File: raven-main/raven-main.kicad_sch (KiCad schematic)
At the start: 2 parts, among them U1 TLV3201AIDCKT

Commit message: Created detector circuit
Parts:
- removed D1: BPW34, OptoDevice:Osram_DIL2_4.3x4.65mm_P5.08mm, symbol Sensor_Optical:BPW34
- removed U1: TLV3201AIDCKT, TLV3201AIDCKT:SOT65P210X110-5N, symbol TLV3201AIDCKT:TLV3201AIDCKT
- added U3: ESP32-S3, Package_DFN_QFN:QFN-56-1EP_7x7mm_P0.4mm_EP4x4mm, symbol MCU_Espressif:ESP32-S3
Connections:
- new net: U3.2 (VDD3P3), U3.3 (VDD3P3)
- new net 5V: U3.55 (VDDA), U3.56 (VDDA)
- new net GND: U3.57 (GND)
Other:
- added sheet Detector (raven-detector.kicad_sch)
- added sheet Power (raven-power.kicad_sch)

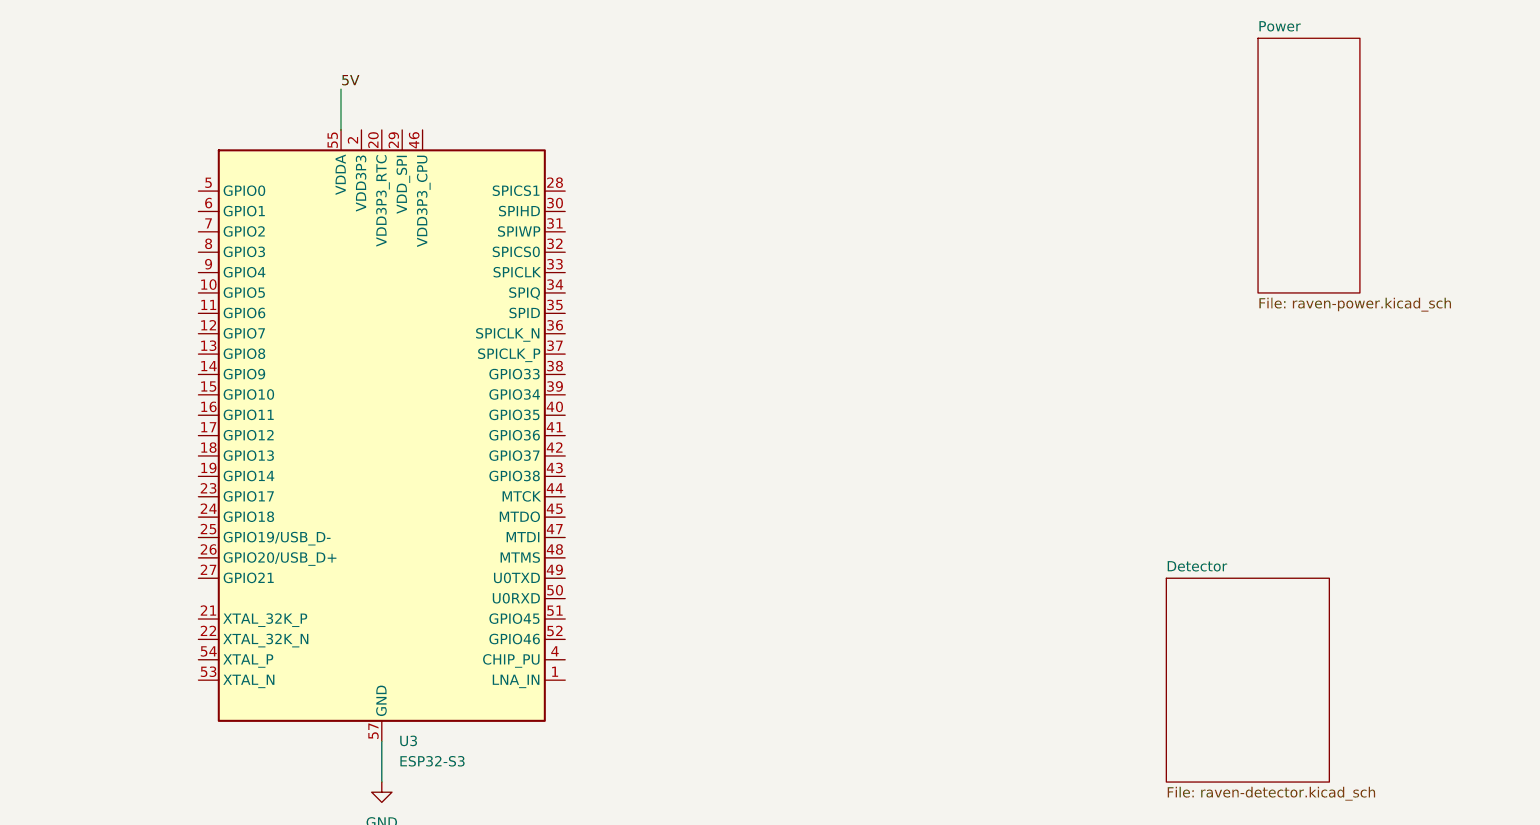
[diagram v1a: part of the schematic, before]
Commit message: Added LDO Regulator
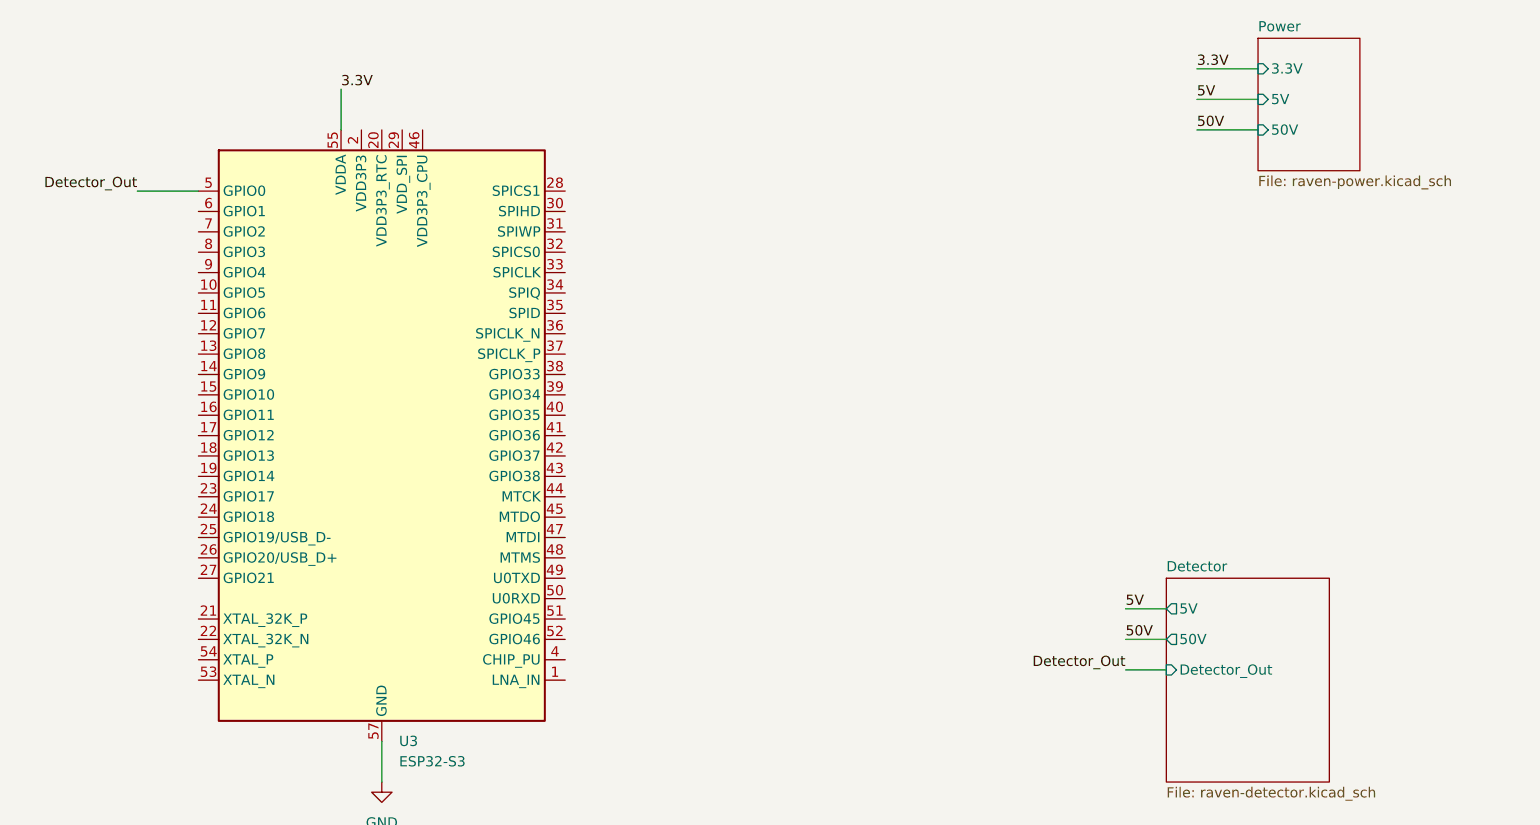
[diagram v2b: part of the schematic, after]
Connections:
- net 5V: no longer U3.55 (VDDA), U3.56 (VDDA)
- net Detector_Out: now reaches U3.5 (GPIO0)
- new net 3.3V: U3.55 (VDDA), U3.56 (VDDA)
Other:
- sheet Detector ports: added 50V, 5V, Detector_Out; removed none
- sheet Power ports: added 3.3V, 50V, 5V; removed none
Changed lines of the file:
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@@
+	(wire
+		(pts
+			(xy 232.41 43.18) (xy 240.03 43.18)
+		)
+		(stroke
+			(width 0)
+			(type default)
+		)
+	)
+	(wire
+		(pts
+			(xy 232.41 46.99) (xy 240.03 46.99)
+		)
+		(stroke
+			(width 0)
+			(type default)
+		)
+	)
 	(wire
 		(pts
@@
 	(wire
 		(pts
+			(xy 223.52 110.49) (xy 228.6 110.49)
+		)
+		(stroke
+			(width 0)
+			(type default)
+		)
+	)
+	(wire
+		(pts
+			(xy 223.52 106.68) (xy 228.6 106.68)
+		)
+		(stroke
+			(width 0)
+			(type default)
+		)
+	)
+	(wire
+		(pts
+			(xy 223.52 114.3) (xy 228.6 114.3)
+		)
+		(stroke
+			(width 0)
+			(type default)
+		)
+	)
+	(wire
+		(pts
 			(xy 125.73 41.91) (xy 125.73 46.99)
 		)
@@
 		)
 	)
+	(wire
+		(pts
+			(xy 100.33 54.61) (xy 107.95 54.61)
+		)
+		(stroke
+			(width 0)
+			(type default)
+		)
+	)
+	(wire
+		(pts
+			(xy 232.41 39.37) (xy 240.03 39.37)
+		)
+		(stroke
+			(width 0)
+			(type default)
+		)
+	)
+	(label "3.3V"
+		(at 232.41 39.37 0)
+		(effects
+			(font
+				(size 1.27 1.27)
+			)
+			(justify left bottom)
+		)
+	)
 	(label "5V"
+		(at 223.52 106.68 0)
+		(effects
+			(font
+				(size 1.27 1.27)
+			)
+			(justify left bottom)
+		)
+	)
+	(label "5V"
+		(at 232.41 43.18 0)
+		(effects
+			(font
+				(size 1.27 1.27)
+			)
+			(justify left bottom)
+		)
+	)
+	(label "50V"
+		(at 232.41 46.99 0)
+		(effects
+			(font
+				(size 1.27 1.27)
+			)
+			(justify left bottom)
+		)
+	)
+	(label "Detector_Out"
+		(at 223.52 114.3 180)
+		(effects
+			(font
+				(size 1.27 1.27)
+			)
+			(justify right bottom)
+		)
+	)
+	(label "3.3V"
 		(at 125.73 41.91 0)
+		(effects
+			(font
+				(size 1.27 1.27)
+			)
+			(justify left bottom)
+		)
+	)
+	(label "Detector_Out"
+		(at 100.33 54.61 180)
+		(effects
+			(font
+				(size 1.27 1.27)
+			)
+			(justify right bottom)
+		)
+	)
+	(label "50V"
+		(at 223.52 110.49 0)
 		(effects
 			(font
@@
 			)
 		)
+		(pin "5V" output
+			(at 228.6 106.68 180)
+			(effects
+				(font
+					(size 1.27 1.27)
+				)
+				(justify left)
+			)
+		)
+		(pin "50V" output
+			(at 228.6 110.49 180)
+			(effects
+				(font
+					(size 1.27 1.27)
+				)
+				(justify left)
+			)
+		)
+		(pin "Detector_Out" input
+			(at 228.6 114.3 180)
+			(effects
+				(font
+					(size 1.27 1.27)
+				)
+				(justify left)
+			)
+		)
 		(instances
 			(project "raven-main"
@@
 	(sheet
 		(at 240.03 35.56)
-		(size 12.7 31.75)
+		(size 12.7 16.51)
 		(exclude_from_sim no)
 		(in_bom yes)
@@
 		)
 		(property "Sheetfile" "raven-power.kicad_sch"
-			(at 240.03 67.8946 0)
+			(at 240.03 52.6546 0)
 			(show_name no)
 			(do_not_autoplace no)
@@
 			)
 		)
+		(pin "3.3V" input
+			(at 240.03 39.37 180)
+			(effects
+				(font
+					(size 1.27 1.27)
+				)
+				(justify left)
+			)
+		)
+		(pin "5V" input
+			(at 240.03 43.18 180)
+			(effects
+				(font
+					(size 1.27 1.27)
+				)
+				(justify left)
+			)
+		)
+		(pin "50V" input
+			(at 240.03 46.99 180)
+			(effects
+				(font
+					(size 1.27 1.27)
+				)
+				(justify left)
+			)
+		)

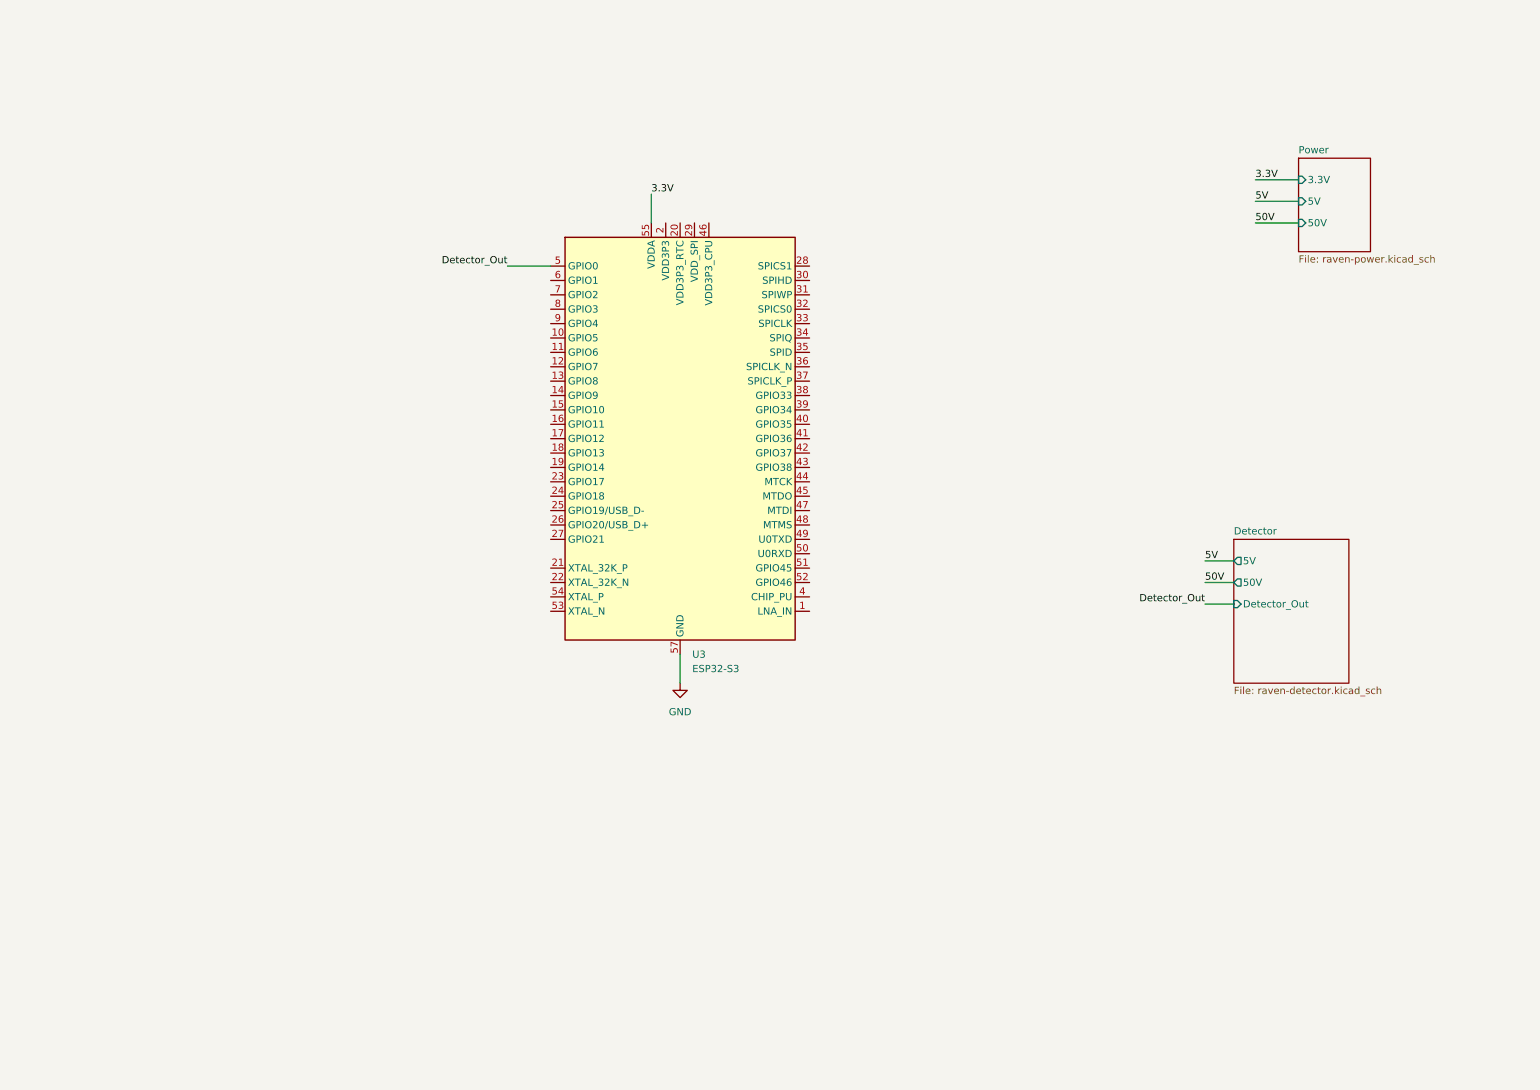
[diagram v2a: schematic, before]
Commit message: Used the ESP-32 board template to create full board
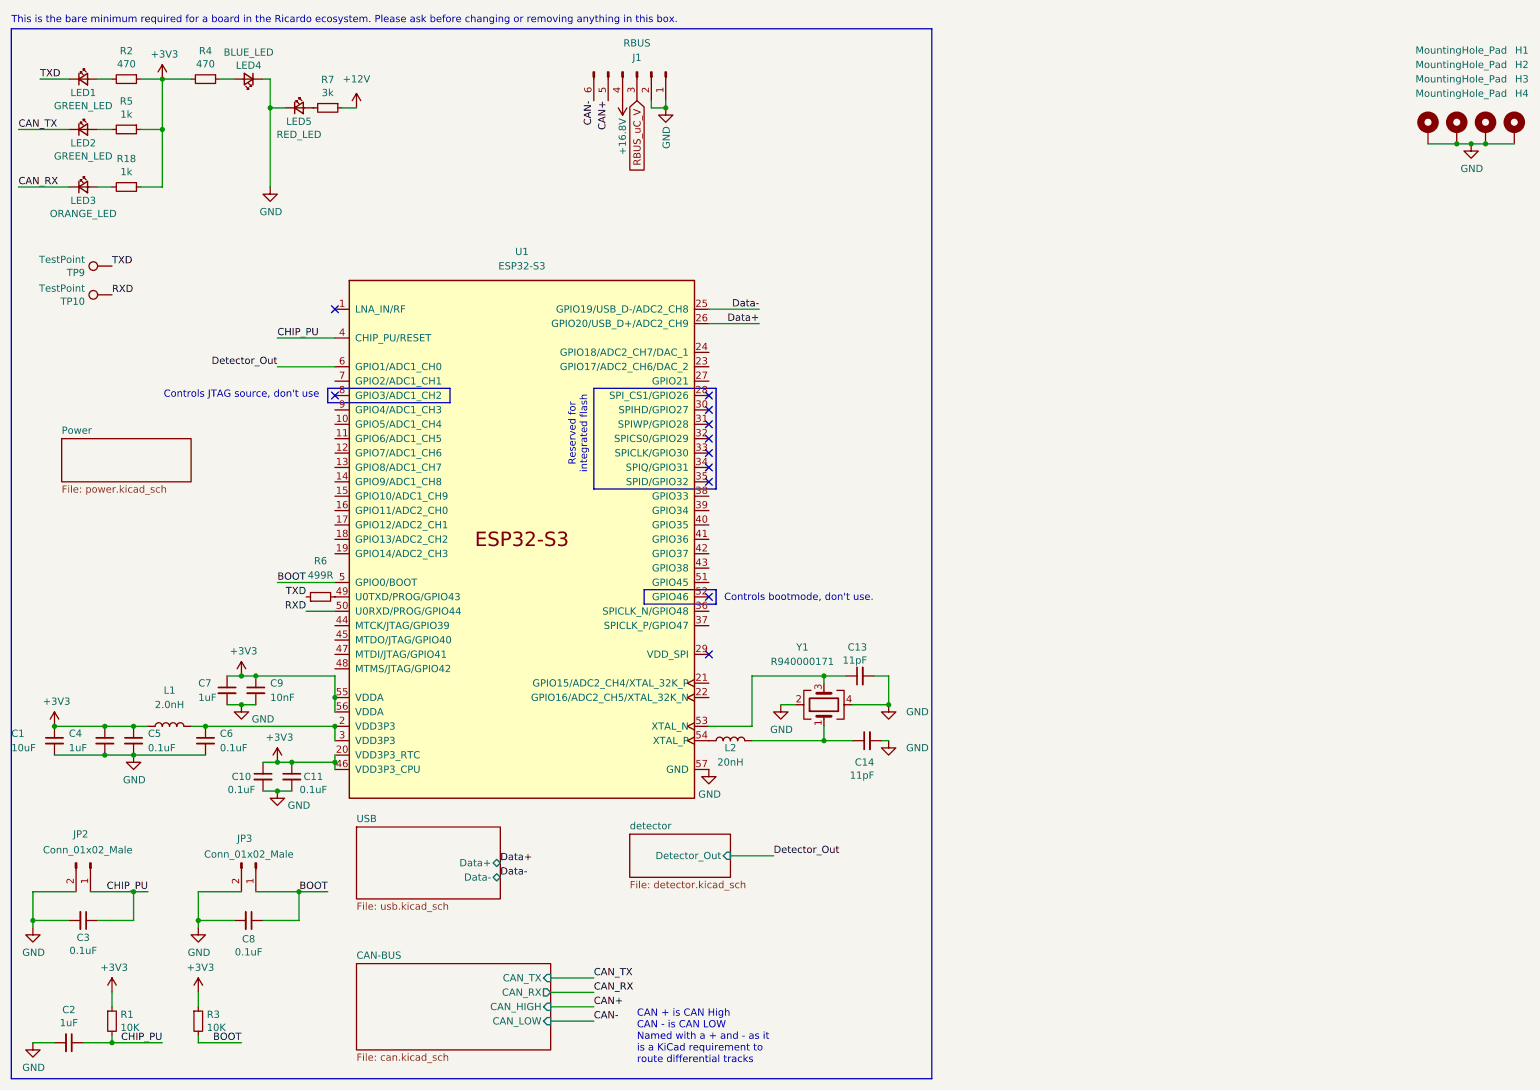
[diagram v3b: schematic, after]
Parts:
- removed U3: ESP32-S3, Package_DFN_QFN:QFN-56-1EP_7x7mm_P0.4mm_EP4x4mm, symbol MCU_Espressif:ESP32-S3
- added C1: 10uF, Capacitor_SMD:C_0402_1005Metric, symbol Device:C_Small
- added C10, C11, C3, C5, C6, C8: 0.1uF, Capacitor_SMD:C_0402_1005Metric, symbol Device:C_Small
- added C13, C14: 11pF, Capacitor_SMD:C_0402_1005Metric, symbol Device:C_Small
- added C2, C4, C7: 1uF, Capacitor_SMD:C_0402_1005Metric, symbol Device:C_Small
- added C9: 10nF, Capacitor_SMD:C_0402_1005Metric, symbol Device:C_Small
- added H1, H2, H3, H4: MountingHole_Pad, MountingHole:MountingHole_3.2mm_M3_DIN965_Pad, symbol Mechanical:MountingHole_Pad
- added J1: RBUS, iclr:Molex_Mini-Fit_Jr_5569-06A2_2x03_P4.20mm_Horizontal, symbol Connector:Conn_01x06_Male
- added JP2, JP3: Conn_01x02_Male, Connector_PinHeader_2.54mm:PinHeader_1x02_P2.54mm_Vertical, symbol Connector:Conn_01x02_Male
- added L1: 2.0nH, Inductor_SMD:L_0402_1005Metric, symbol Device:L
- added L2: 20nH, Inductor_SMD:L_0402_1005Metric, symbol Device:L
- added LED1, LED2: GREEN_LED, LED_SMD:LED_0402_1005Metric, symbol Device:LED_Small
- added LED3: ORANGE_LED, LED_SMD:LED_0402_1005Metric, symbol Device:LED_Small
- added LED4: BLUE_LED, LED_SMD:LED_0402_1005Metric, symbol Device:LED_Small
- added LED5: RED_LED, LED_SMD:LED_0402_1005Metric, symbol Device:LED_Small
- added R1, R3: 10K, Resistor_SMD:R_0402_1005Metric, symbol Device:R_Small
- added R18, R5: 1k, Resistor_SMD:R_0402_1005Metric, symbol Device:R_Small
- added R2, R4: 470, Resistor_SMD:R_0402_1005Metric, symbol Device:R_Small
- added R6: 499R, Resistor_SMD:R_0402_1005Metric, symbol Device:R_Small
- added R7: 3k, Resistor_SMD:R_0402_1005Metric, symbol Device:R_Small
- added TP10, TP9: TestPoint, TestPoint:TestPoint_Pad_D1.0mm, symbol Connector:TestPoint
- added U1: ESP32-S3, iclr:QFN40P700X700X90-57N, symbol Espressif:ESP32-S3
- added Y1: R940000171, iclr:Crystal_SMD_2016-4Pin_2.0x1.6mm, symbol Device:Crystal_GND24
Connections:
- net Detector_Out: now also U1.6 (GPIO1/ADC1_CH0)
- net GND: now also C1.2, C10.2, C11.2, C13.2, C14.2, C2.2, C3.2, C4.2, C5.2, C6.2, C7.2, C8.2, C9.2, H1.1, H2.1, H3.1, H4.1, J1.1 (Pin_1), J1.2 (Pin_2), JP2.2 (Pin_2), JP3.2 (Pin_2), LED4.1 (K), LED5.1 (K), U1.57 (GND), Y1.2, Y1.4
- new net: LED1.2 (A), R2.2
- new net: LED4.2 (A), R4.1
- new net: LED5.2 (A), R7.2
- new net: LED2.2 (A), R5.2
- new net: LED3.2 (A), R18.2
- new net: C14.1, L2.2, Y1.1
- new net: C13.1, U1.53 (XTAL_N), Y1.3
- new net: L2.1, U1.54 (XTAL_P)
- new net: C6.1, L1.2, U1.2 (VDD3P3), U1.3 (VDD3P3)
- new net: R6.2, U1.49 (U0TXD/PROG/GPIO43)
- new net +12V: R7.1
- new net +16.8V: J1.4 (Pin_4)
- new net +3V3: C1.1, C10.1, C11.1, C4.1, C5.1, C7.1, C9.1, L1.1, R1.1, R18.1, R2.1, R3.1, R4.2, R5.1, U1.20 (VDD3P3_RTC), U1.46 (VDD3P3_CPU), U1.55 (VDDA), U1.56 (VDDA)
- new net BOOT: C8.1, JP3.1 (Pin_1), R3.2, U1.5 (GPIO0/BOOT)
- new net CAN+: J1.5 (Pin_5)
- new net CAN-: J1.6 (Pin_6)
- new net CAN_RX: LED3.1 (K)
- new net CAN_TX: LED2.1 (K)
- new net CHIP_PU: C2.1, C3.1, JP2.1 (Pin_1), R1.2, U1.4 (CHIP_PU/RESET)
- new net Data+: U1.26 (GPIO20/USB_D+/ADC2_CH9)
- new net Data-: U1.25 (GPIO19/USB_D-/ADC2_CH8)
- new net RBUS_uC_V: J1.3 (Pin_3)
- new net RXD: TP10.1, U1.50 (U0RXD/PROG/GPIO44)
- new net TXD: LED1.1 (K), R6.1, TP9.1
- no-connect marks 0 -> 11
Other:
- removed sheet Detector
- added sheet CAN-BUS (can.kicad_sch)
- added sheet USB (usb.kicad_sch)
- added sheet detector (detector.kicad_sch)
- sheet Power: file raven-power.kicad_sch -> power.kicad_sch
- sheet Power ports: added none; removed 3.3V, 50V, 5V
- note added: "CAN + is CAN High CAN - is CAN LOW Named with a + and - as it is a KiCad requirement to route differential tracks"
- note added: "Controls JTAG source, don't use"
- note added: "Controls bootmode, don't use."
- note added: "Reserved for integrated flash"
- note added: "This is the bare minimum required for a board in the Ricardo ecosystem. Please ask before changing or removing anything in this box."
